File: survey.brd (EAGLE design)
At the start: 97.8 x 50.5 mm, 20 parts

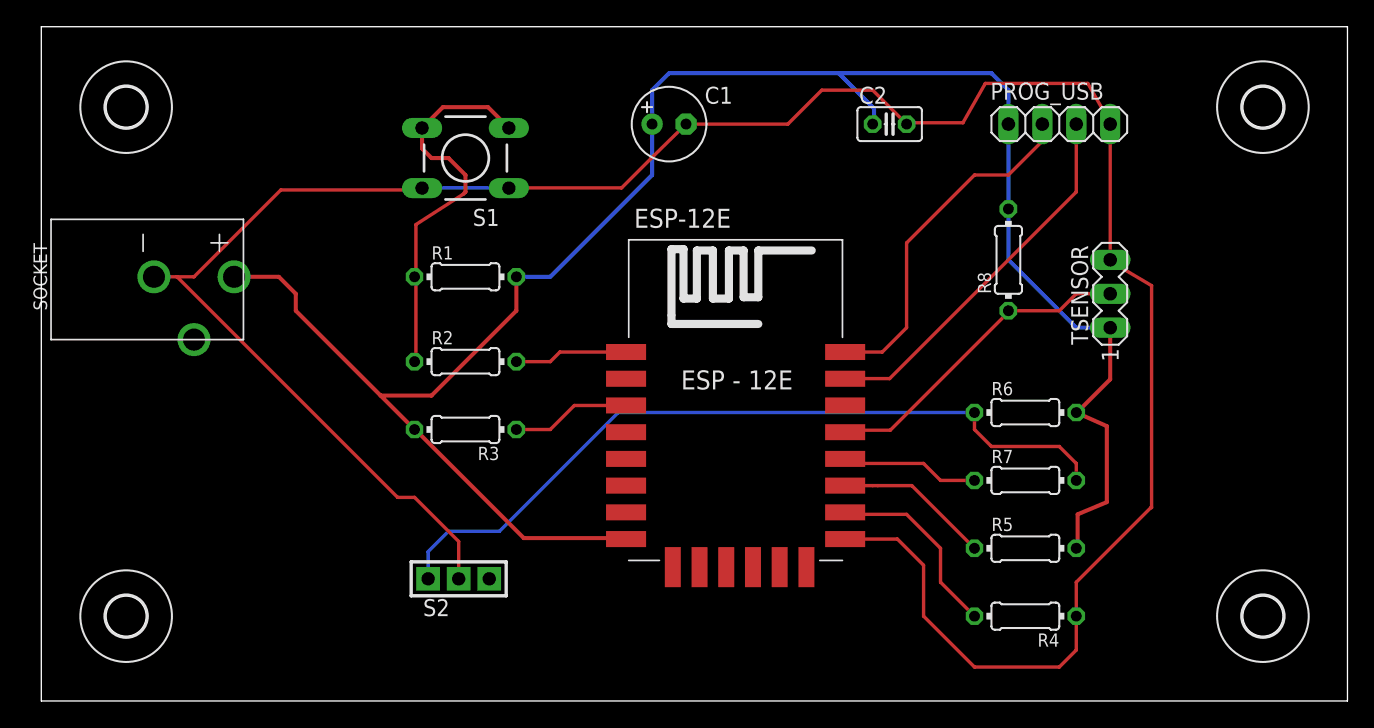
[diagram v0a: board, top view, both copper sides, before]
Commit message: Corrected programming switch connection.
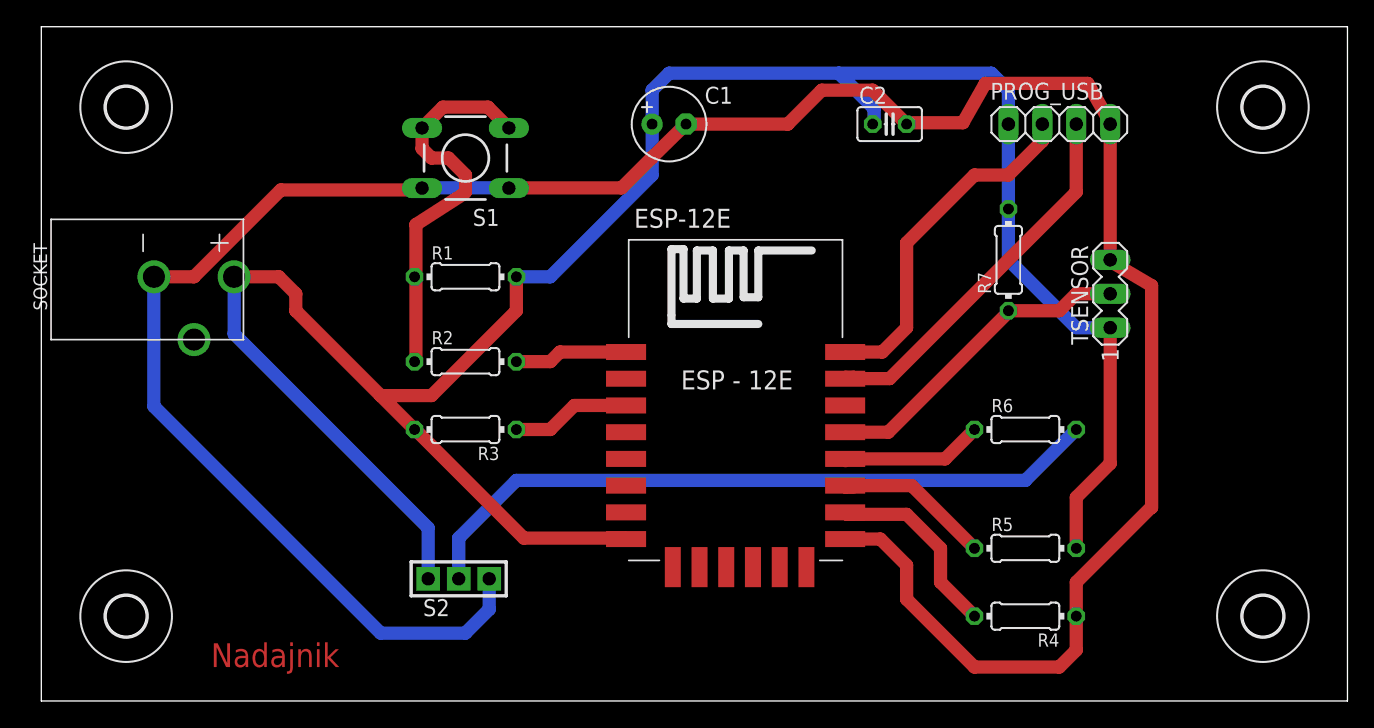
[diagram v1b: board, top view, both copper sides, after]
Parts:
- removed R8: 4,7k, rcl:0204/7
- R7: value 100 -> 4,7k
- moved R7 16.6 mm to (72.4, 82.5), turned to 90 degrees
- moved R6 1.27 mm to (73.7, 69.8)
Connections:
- net GND: now also S2.P$3; no longer S2.P$2
- net N$10: now also R6.1; no longer R7.1
- net N$5: now also R7.1; no longer R8.1
- net N$6: now also R6.2, S2.P$2; no longer R6.1, R7.2, S2.P$1
- net VCC: now also R7.2, S2.P$1; no longer R6.2, R8.2
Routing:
- net VCC: track 149.3 -> 174.9 mm
- net GND: track 182.2 -> 194.2 mm
- net N$6: track 58.7 -> 52.6 mm
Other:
- board text added: "Nadajnik"
